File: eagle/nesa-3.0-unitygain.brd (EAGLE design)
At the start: 65 x 42 mm, 15 parts, among them IC1 OPA4134

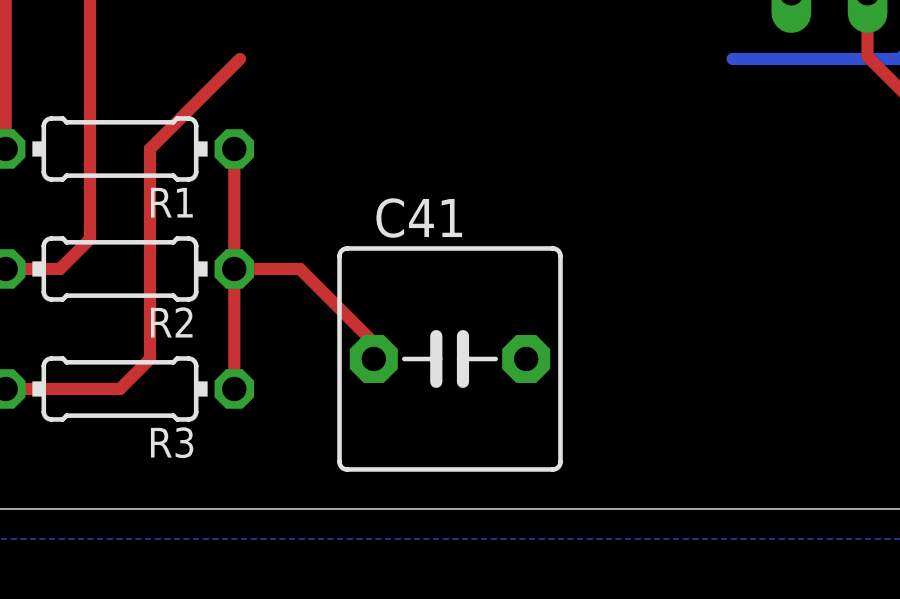
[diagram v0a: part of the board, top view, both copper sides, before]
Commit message: Some minor changes to unitygain schematics
Don't use these schematics yet :)
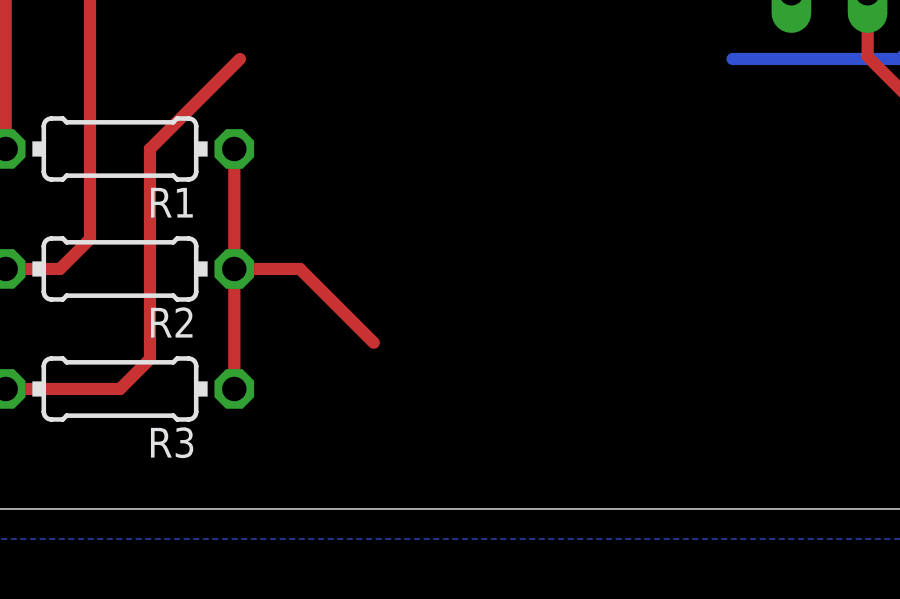
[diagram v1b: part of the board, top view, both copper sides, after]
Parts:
- removed C41: 1uF, capacitor-wima:C5B7.2
- R1, R2, R3: value 2k -> 10k
- R42: value 1k -> 10k
- R43: value 10k -> 20k
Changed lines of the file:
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@@
 <element name="C2" library="resistor" package="E3,5-10" value="1000uF" x="7" y="20" rot="R270"/>
 <element name="JP2" library="pinhead" package="1X03" value="J2" x="4" y="8" rot="R90"/>
-<element name="C41" library="capacitor-wima" package="C5B7.2" value="1uF" x="27" y="5"/>
 <element name="R41" library="resistor" package="0204/7" value="100k" x="53" y="5" rot="R180"/>
-<element name="R42" library="resistor" package="0204/7" value="1k" x="56" y="13" rot="R180"/>
-<element name="R43" library="resistor" package="0204/7" value="10k" x="55" y="9" rot="R180"/>
+<element name="R42" library="resistor" package="0204/7" value="10k" x="56" y="13" rot="R180"/>
+<element name="R43" library="resistor" package="0204/7" value="20k" x="55" y="9" rot="R180"/>
 <element name="JP3" library="pinhead" package="2X04" value="" x="61" y="21" rot="R270"/>
-<element name="R1" library="resistor" package="0204/7" value="2k" x="16" y="12" rot="R180"/>
-<element name="R2" library="resistor" package="0204/7" value="2k" x="16" y="8" rot="R180"/>
-<element name="R3" library="resistor" package="0204/7" value="2k" x="16" y="4" rot="R180"/>
+<element name="R1" library="resistor" package="0204/7" value="10k" x="16" y="12" rot="R180"/>
+<element name="R2" library="resistor" package="0204/7" value="10k" x="16" y="8" rot="R180"/>
+<element name="R3" library="resistor" package="0204/7" value="10k" x="16" y="4" rot="R180"/>
 </elements>
 <signals>
